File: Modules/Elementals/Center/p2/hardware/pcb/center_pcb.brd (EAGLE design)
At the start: 17.8 x 100 mm, 24 parts, among them J1 WQP-PJ398SM6, J10 WQP-PJ398SM6, J11 WQP-PJ398SM6, J12 WQP-PJ398SM6, J2 WQP-PJ398SM6, J3 WQP-PJ398SM6, J4 WQP-PJ398SM6, J5 WQP-PJ398SM6, J6 WQP-PJ398SM6, J7 WQP-PJ398SM6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

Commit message: Added panel ref, resized
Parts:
- added U$1: (no value), SonicAthame:LOGO-65MIL-BSILK
- added U$2: (no value), SonicAthame:PANEL_REF_4U
- moved C1 11.5 mm to (8.89, 102.9)
- moved J1 11.5 mm to (5.08, 95.2)
- moved J2 11.5 mm to (15.2, 95.2)
- moved J3 11.5 mm to (5.08, 80.0)
- moved J4 11.5 mm to (15.2, 80.0)
- moved R1 11.5 mm to (14.6, 102.9)
- moved C6 11.5 mm to (8.89, 26.7)
- moved R6 11.5 mm to (14.6, 26.7)
- moved C3 11.5 mm to (8.89, 72.4)
- moved C4 11.5 mm to (8.89, 57.1)
- moved J10 11.5 mm to (15.2, 34.3)
- moved J11 11.5 mm to (5.08, 19.1)
- moved J12 11.5 mm to (15.2, 19.1)
- moved J7 11.5 mm to (5.08, 49.5)
- moved J8 11.5 mm to (15.2, 49.5)
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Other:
- board size 17.8 x 100 mm -> 17.8 x 93.7 mm
- board text removed: "Sonic Athame™"
- board text removed: "The Point of Modular"

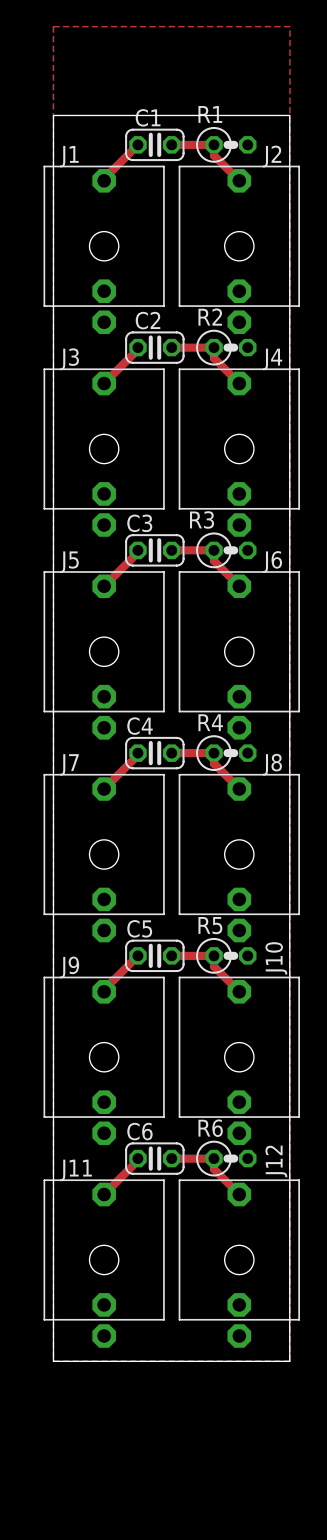
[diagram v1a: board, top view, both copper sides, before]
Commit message: Elemental Center PCB ready
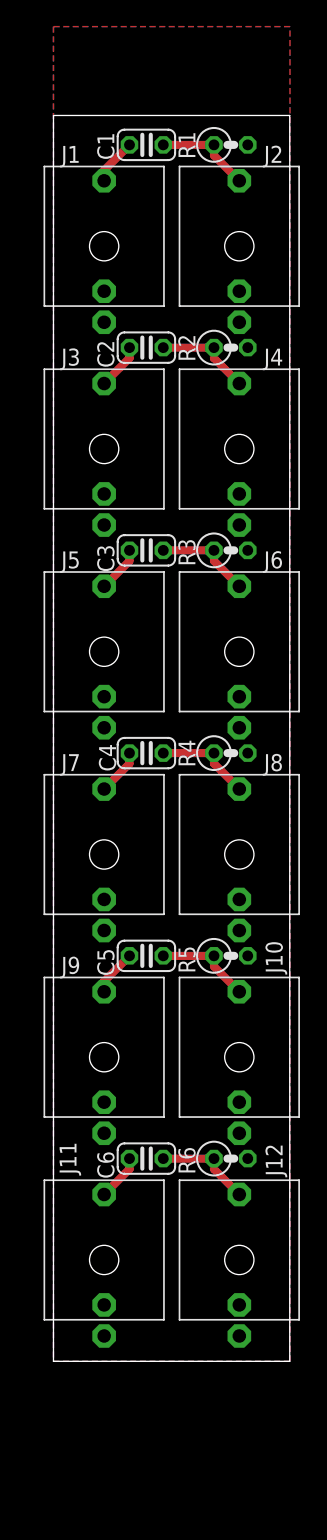
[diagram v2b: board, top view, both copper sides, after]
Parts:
- removed U$1: (no value), SonicAthame:LOGO-65MIL-BSILK
- added U$3: (no value), SonicAthame:LOGO-65MIL-TSILK
- moved C1 0.63 mm to (8.26, 102.9)
- moved C2 0.63 mm to (8.26, 87.6)
- moved C3 0.63 mm to (8.26, 72.4)
- moved C4 0.63 mm to (8.26, 57.1)
- moved C5 0.63 mm to (8.26, 41.9)
- moved C6 0.63 mm to (8.26, 26.7)
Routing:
- net N$8: track 6.66 -> 7.30 mm
- net N$5: track 6.66 -> 7.30 mm
- net N$3: track 6.66 -> 7.30 mm
- net N$2: track 6.66 -> 7.30 mm
- net N$11: track 6.66 -> 7.30 mm
- net N$10: track 6.66 -> 7.30 mm
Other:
- board text added: "For schematics, Gerber files, build instructions, and other arcane resources, go to sonic-athame.com"
- board text removed: "Sonic Athame is fully open-hardware and open-software! Find schematics and code on the official GitHub: github.com/nimaid/Sonic-Athame-eurorack"

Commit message: Finalized center v2
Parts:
- moved R1 0.63 mm to (15.2, 102.9)
- moved R2 0.63 mm to (15.2, 87.6)
- moved R3 0.63 mm to (15.2, 72.4)
- moved R4 0.63 mm to (15.2, 57.1)
- moved R5 0.63 mm to (15.2, 41.9)
- moved R6 0.63 mm to (15.2, 26.7)
